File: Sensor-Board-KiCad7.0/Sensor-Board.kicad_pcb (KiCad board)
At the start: 2 copper layers, 75.4 x 75.4 mm, 128 parts, among them J2 B04B-XASK-1, U1 OPA396DCKT, U10 BME680, U11 OPA396DCKT, U12 OPA396DCKT, U14 OPA396DCKT, U15 MMBFJ177LT1, U16 MMBFJ177LT1, U17 MMBFJ177LT1, U18 NAU7802SGI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

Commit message: Cleaned up some traces
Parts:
- moved R21 0.48 mm to (101.0, 114.5)
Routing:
- net +3.3V: track 452.5 -> 470.3 mm, vias 15 -> 17
- net Ref2_CO: track 45.4 -> 51.5 mm
- net Count2_SO2: track 47.0 -> 50.7 mm
- net 680_SCL1: track 133.4 -> 136.6 mm
- net 680_SDA1: track 43.9 -> 46.7 mm
- net ADC3_SDA: track 38.8 -> 41.0 mm
- net Net-(U32-SD3): track 115.1 -> 117.2 mm
- net Net-(U32-SD1): track 25.8 -> 24.7 mm
- net GND: track 180.2 -> 179.2 mm, vias 30 -> 32
- net Net-(U32-SD0): track 77.4 -> 76.4 mm
- net Net-(U32-SC3): track 103.0 -> 104.0 mm
- net Net-(U32-SC1): track 25.0 -> 24.1 mm
- net 680_SDA2: track 135.5 -> 136.2 mm
- net Net-(U5-VIN2N): track 9.82 -> 10.5 mm
- net Count2_CO: track 63.3 -> 64.0 mm
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
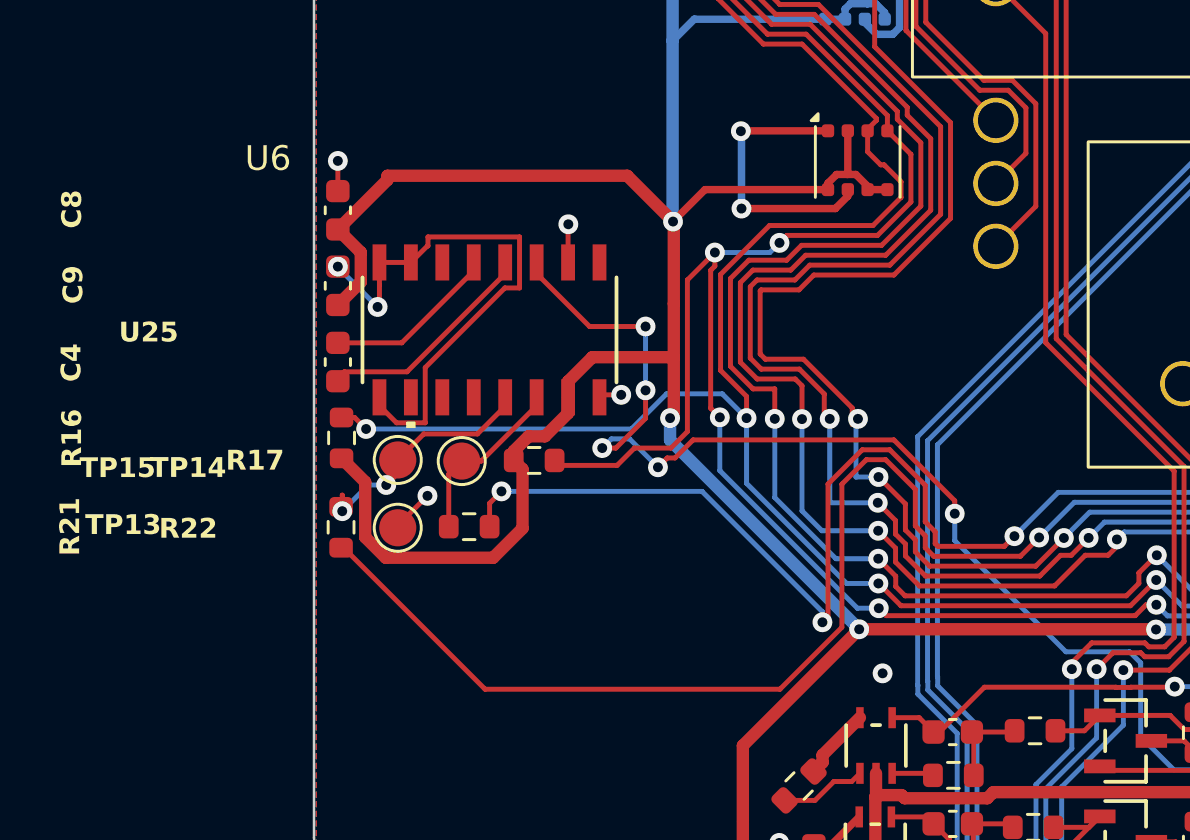
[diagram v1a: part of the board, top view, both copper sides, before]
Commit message: Pushed row with C8, C9, etc. down to create more clearance for gas collection cell
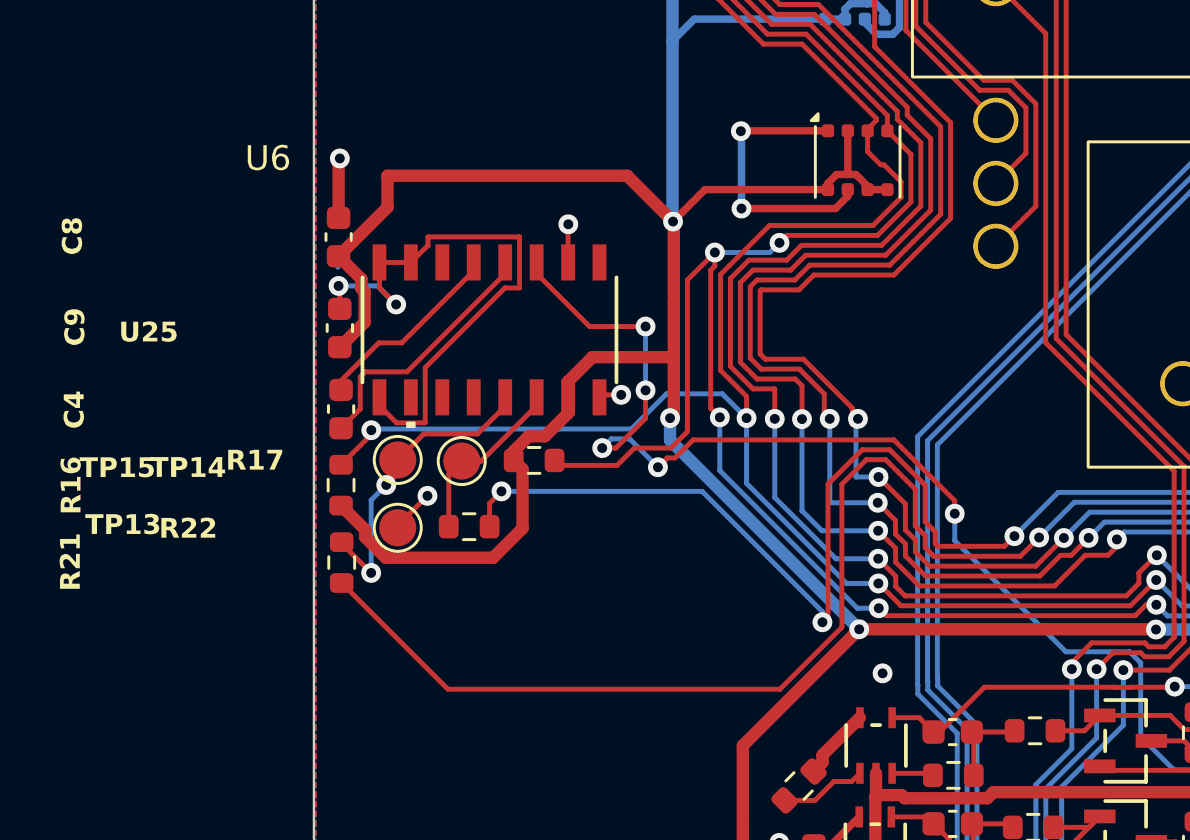
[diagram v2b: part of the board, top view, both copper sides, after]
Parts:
- moved R16 1.91 mm to (101.0, 112.8)
- moved C4 1.90 mm to (101.0, 109.8)
- moved C9 1.71 mm to (101.0, 106.5)
- moved R21 1.43 mm to (101.1, 116.0)
- moved C8 1.08 mm to (101.0, 102.8)
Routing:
- net GND: track 179.2 -> 182.5 mm
- net ADC1_SCL: track 10.0 -> 12.7 mm
- net Net-(U25-VIN2N): track 9.13 -> 10.4 mm
- net Net-(U25-VIN2P): track 7.15 -> 7.91 mm
- net Net-(U32-SC0): track 83.0 -> 82.4 mm
- net 680_SDA2: track 136.2 -> 136.7 mm

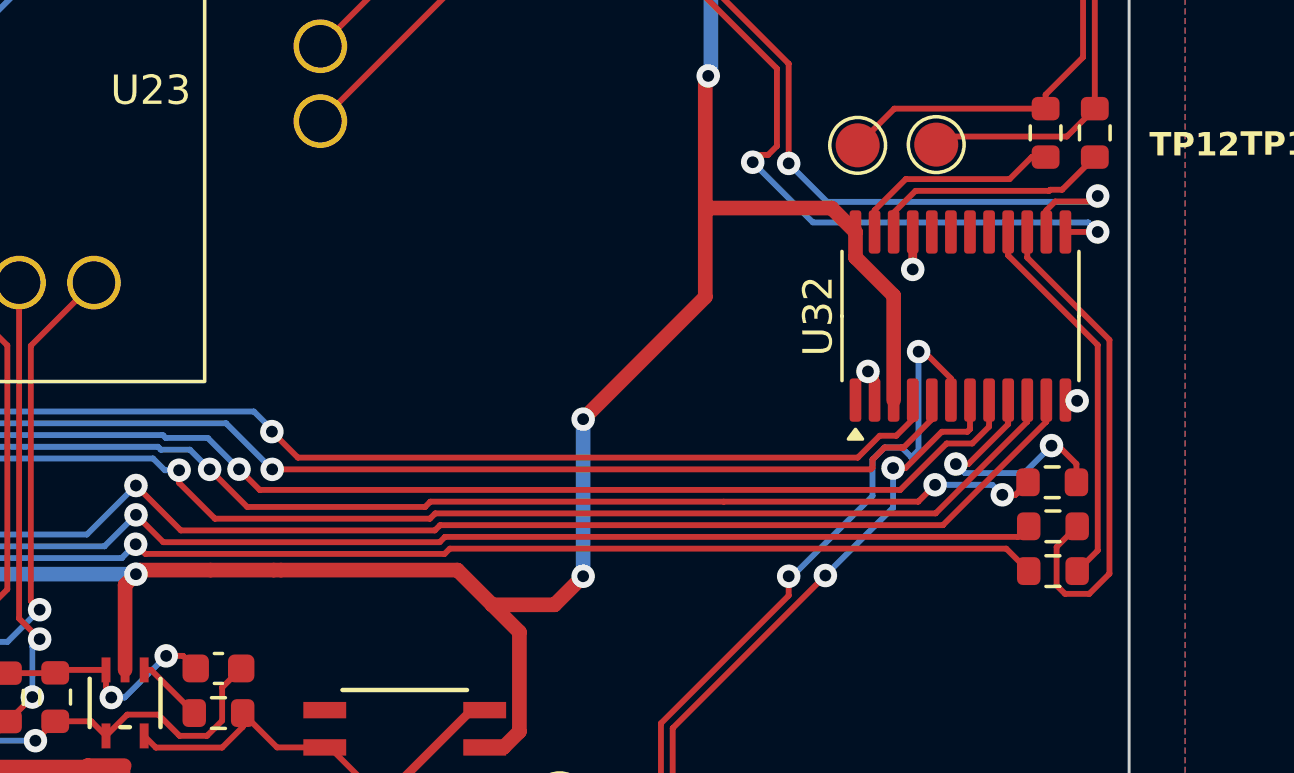
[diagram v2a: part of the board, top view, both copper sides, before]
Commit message: Pushed U32 to the right a bit
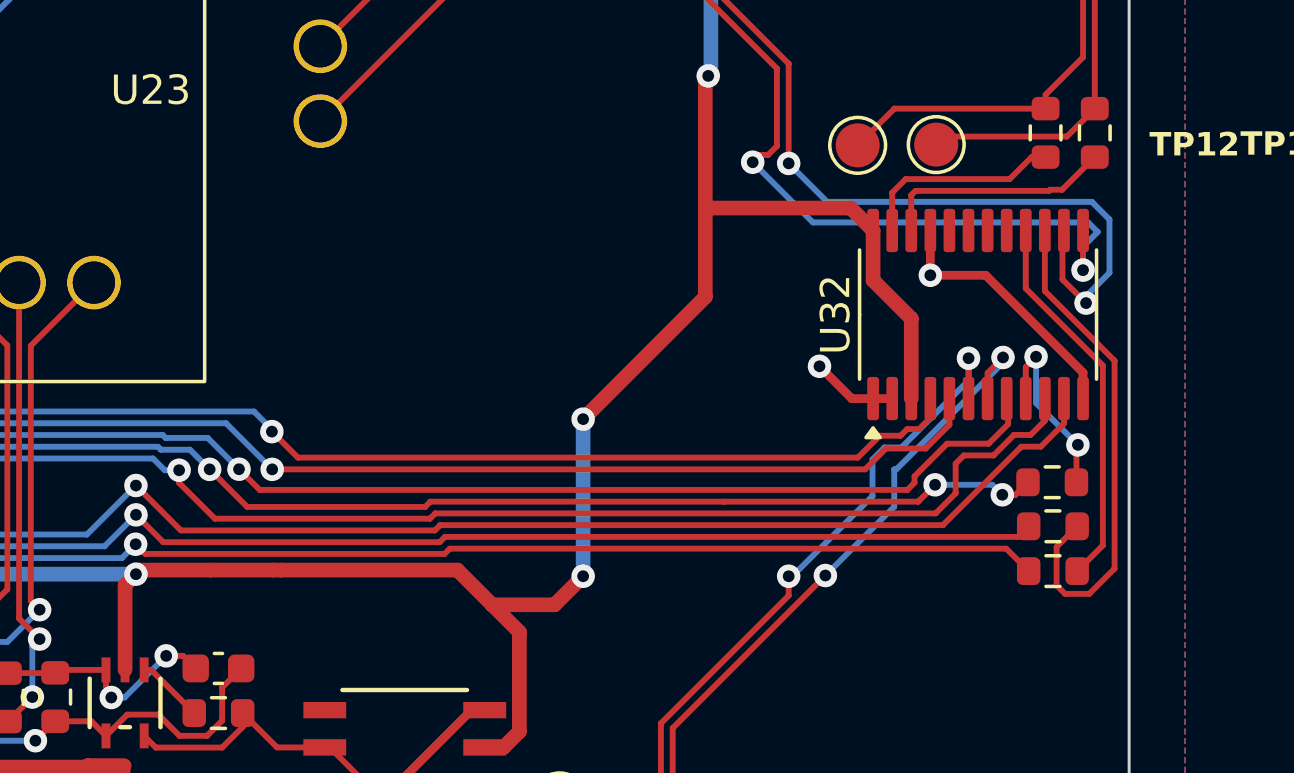
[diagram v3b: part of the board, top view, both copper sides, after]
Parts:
- moved U32 0.60 mm to (170.2, 109.8)
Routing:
- net GND: track 182.5 -> 191.6 mm, vias 32 -> 31
- net Net-(U32-SC4): track 58.7 -> 62.6 mm
- net Net-(U32-SC1): track 24.1 -> 26.9 mm
- net Net-(U32-SC2): track 8.67 -> 6.46 mm
- net Net-(U32-SD4): track 60.0 -> 61.8 mm
- net Net-(U32-SD3): track 117.2 -> 118.5 mm
- net Net-(U32-SD1): track 24.7 -> 23.7 mm
- net Net-(U32-SD2): track 87.9 -> 88.6 mm
- net Net-(U32-SC3): track 104.0 -> 104.7 mm
- net Net-(U32-SD0): track 76.4 -> 77.0 mm
- net Net-(U32-SC0): track 82.4 -> 83.0 mm
- net +3.3V: track 470.2 -> 470.7 mm

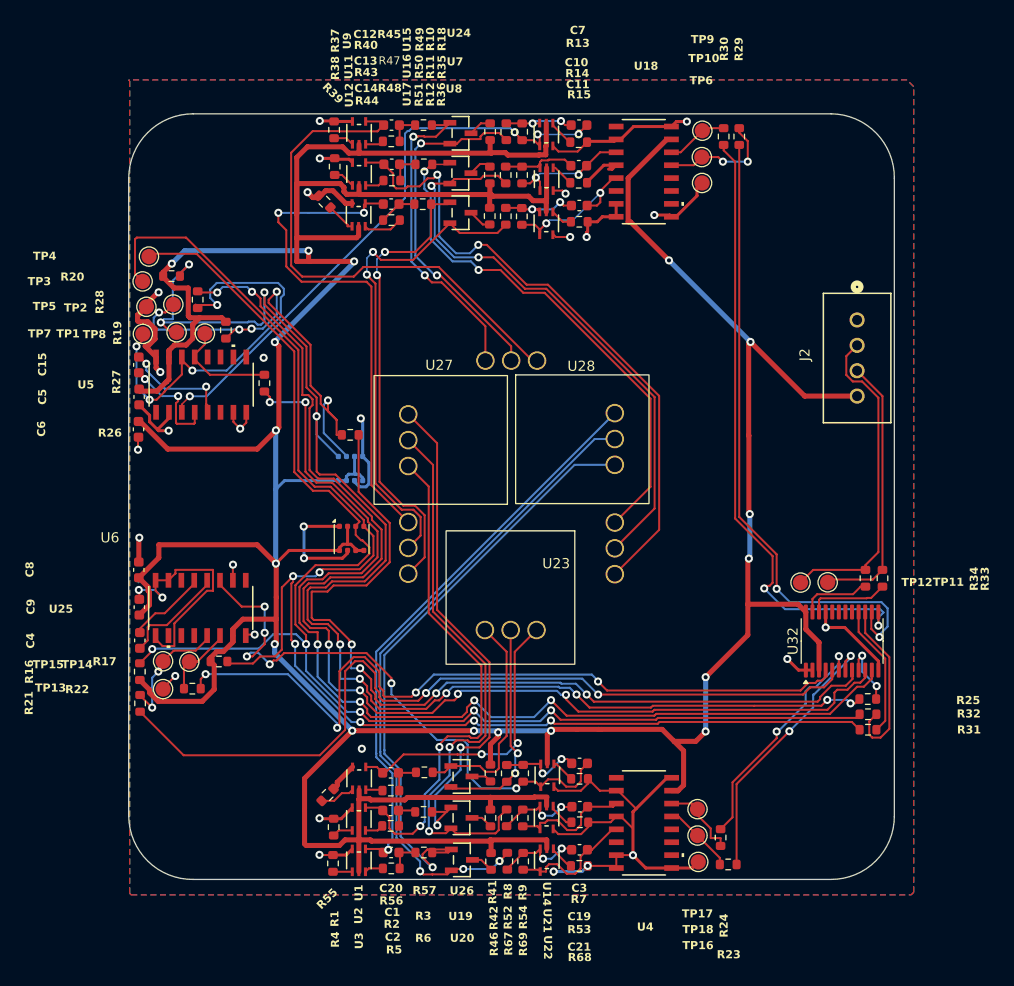
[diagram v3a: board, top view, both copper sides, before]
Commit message: Placed silkscreen
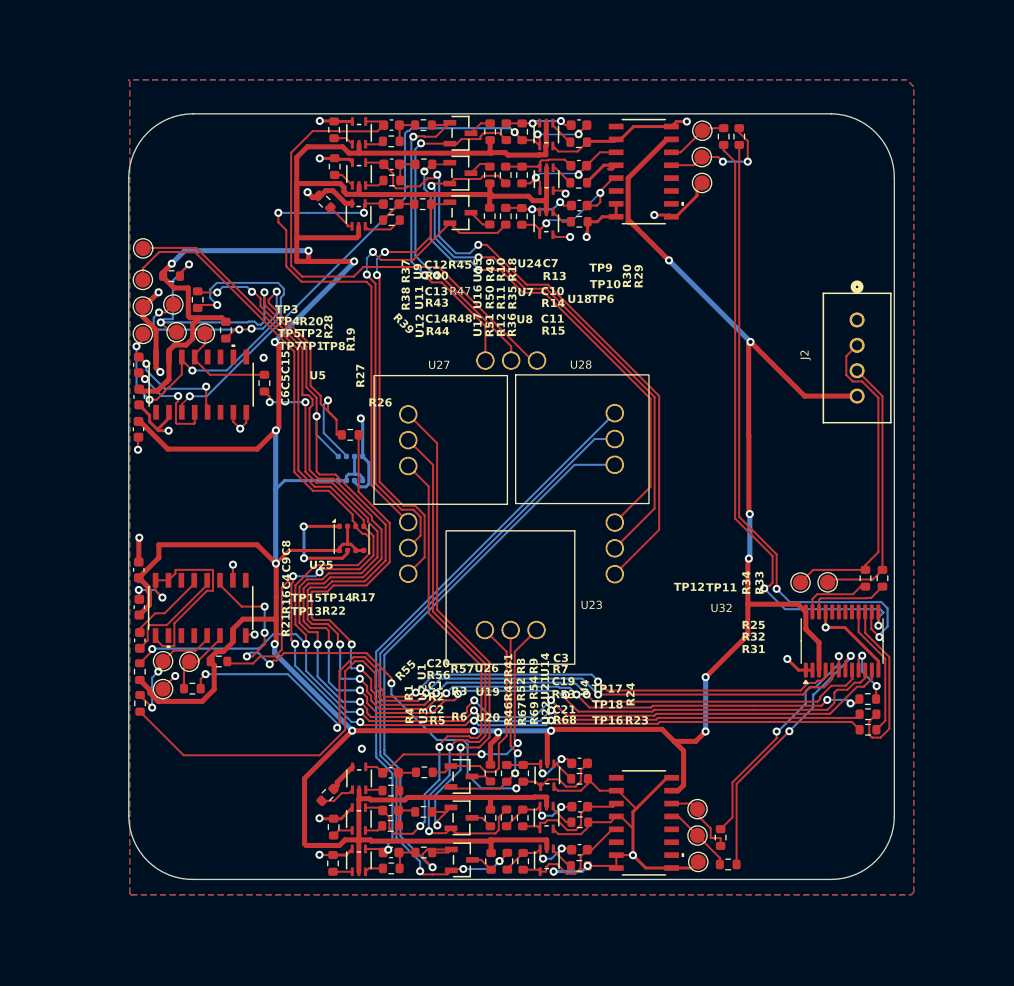
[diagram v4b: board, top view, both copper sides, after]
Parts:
- moved TP3 3.25 mm to (101.4, 71.2)
- moved TP4 2.38 mm to (101.3, 74.2)
- moved TP5 0.35 mm to (101.3, 76.9)
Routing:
- net 680_SCL2: track 140.3 -> 134.5 mm
- net 680_SDA2: track 136.7 -> 138.9 mm
- net GND: track 191.6 -> 189.5 mm

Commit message: Added mounting holes
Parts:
- added H1: MountingHole, Rod_Mounting_Hole_6.7564mm:Rod_Mounting_Hole_6.7564mm, F.Cu at (106.3, 64.2)
- added H2: MountingHole, Rod_Mounting_Hole_6.7564mm:Rod_Mounting_Hole_6.7564mm, F.Cu at (106.3, 127.1)
- added H3: MountingHole, Rod_Mounting_Hole_6.7564mm:Rod_Mounting_Hole_6.7564mm, F.Cu at (106.5, 95.6)
- added H4: MountingHole, Rod_Mounting_Hole_6.7564mm:Rod_Mounting_Hole_6.7564mm, F.Cu at (168.9, 95.6)
- added H5: MountingHole, Rod_Mounting_Hole_6.7564mm:Rod_Mounting_Hole_6.7564mm, F.Cu at (169.1, 64.2)
- added H6: MountingHole, Rod_Mounting_Hole_6.7564mm:Rod_Mounting_Hole_6.7564mm, F.Cu at (169.2, 127.1)

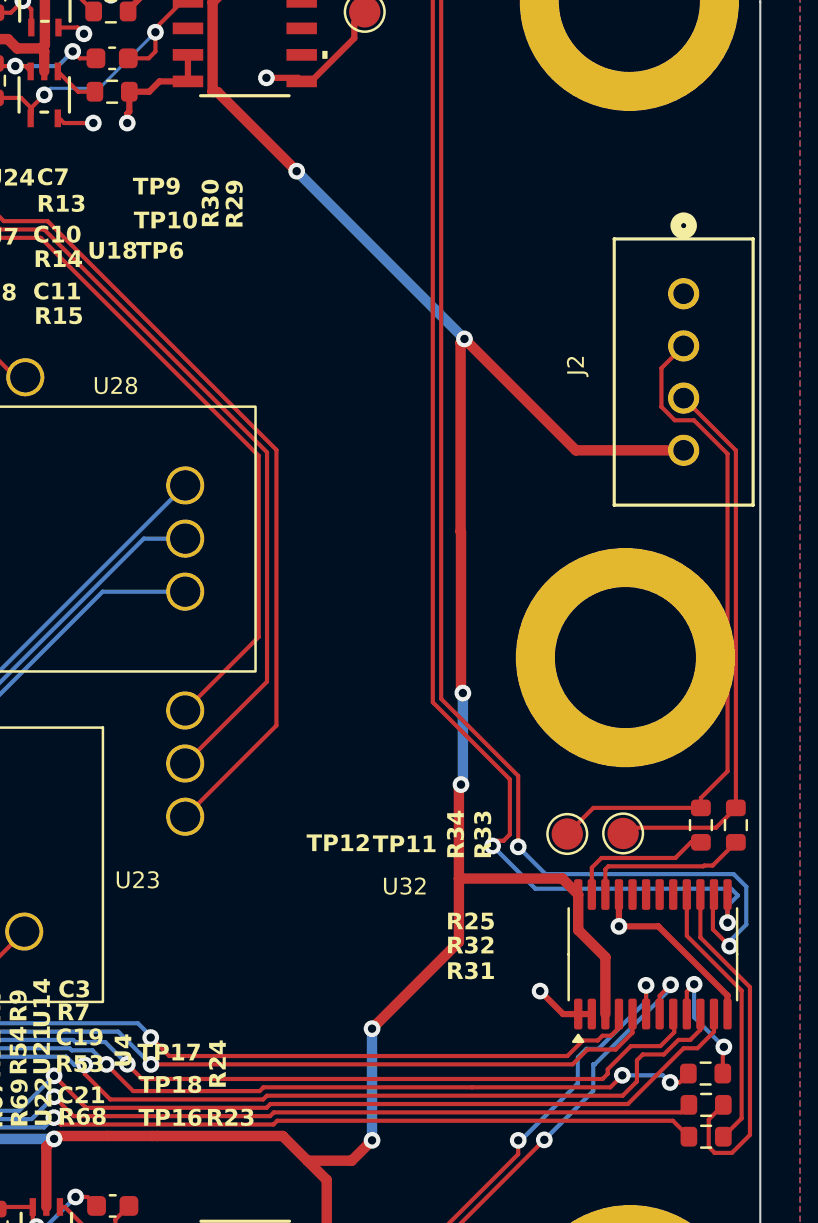
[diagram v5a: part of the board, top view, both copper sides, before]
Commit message: Added logo and contributors to board
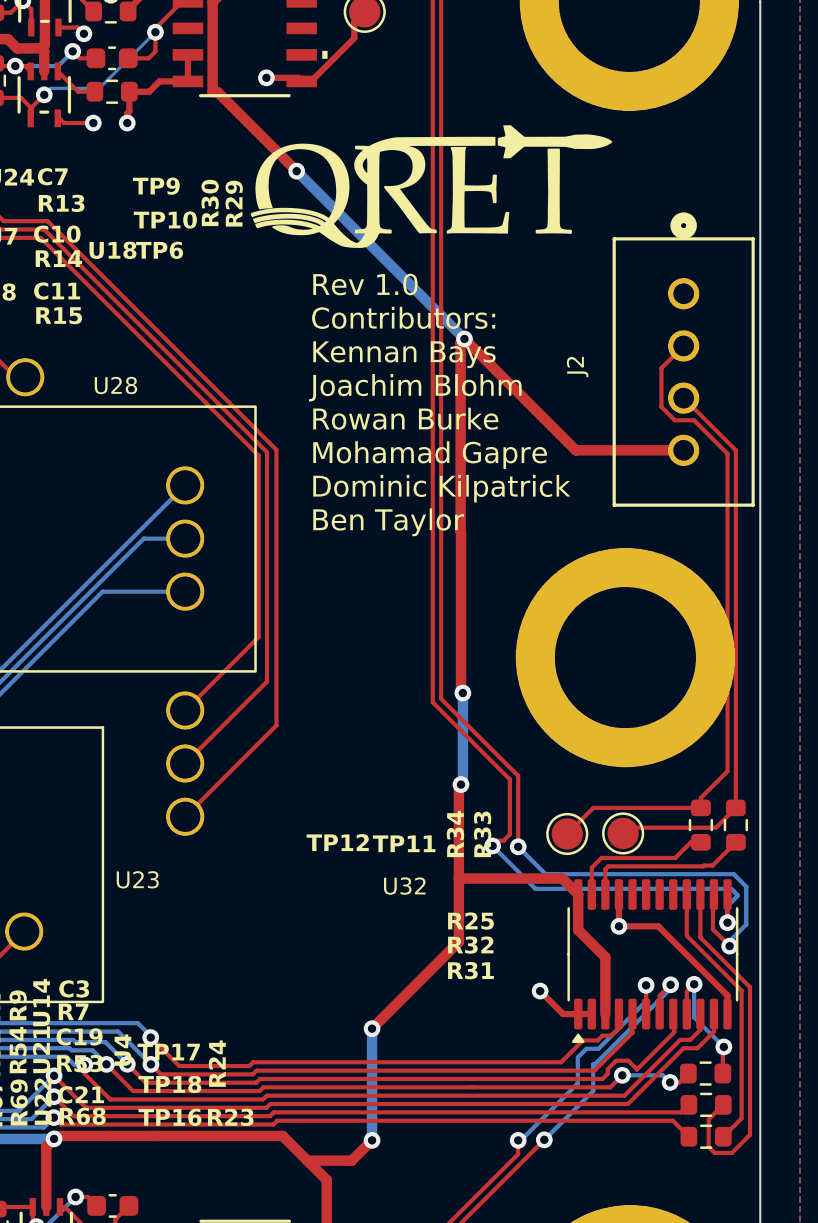
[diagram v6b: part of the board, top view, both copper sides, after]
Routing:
- net Net-(U32-SD3): track 118.5 -> 117.9 mm
- net Net-(U32-SD2): track 88.6 -> 89.2 mm
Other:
- board text added: "Rev 1.0 Contributors: Kennan Bays Joachim Blohm Rowan Burke Mohamad Gapre Dominic Kilpatrick Ben Taylor"
